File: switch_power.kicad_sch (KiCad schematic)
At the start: 0 parts

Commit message: CuPhy: adding ports
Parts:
- added U1: ~, Package_QFP:TQFP-128_14x14mm_P0.4mm, symbol lan9645xF:lan9645xF_128_TQFP

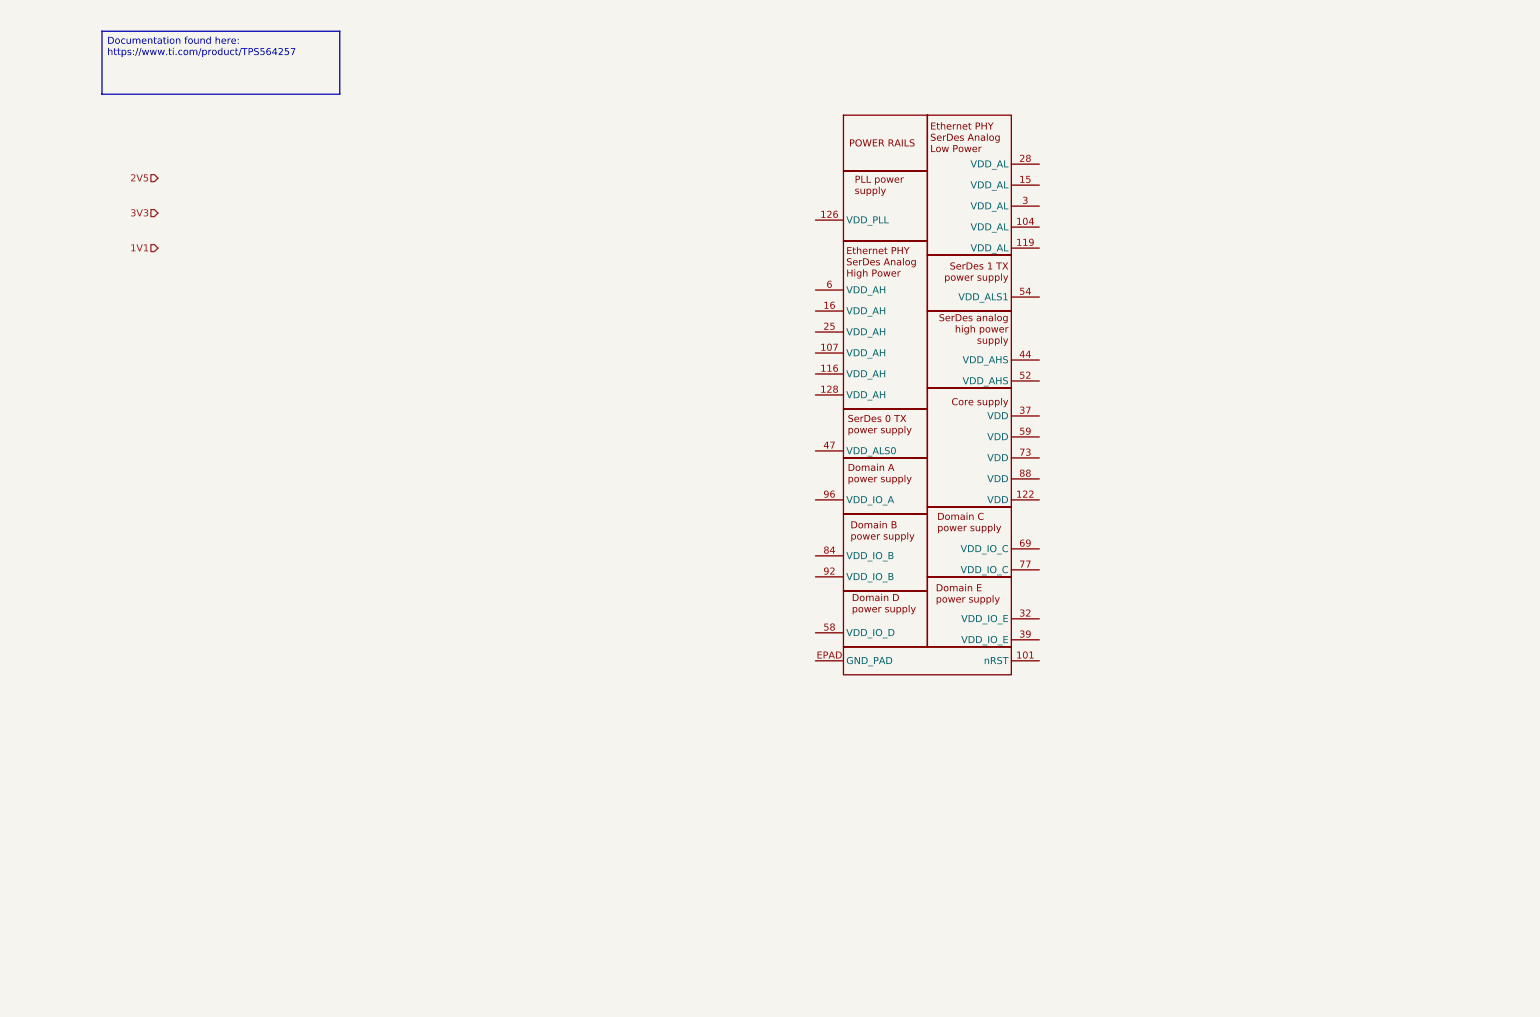
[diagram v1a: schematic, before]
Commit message: schematics: fixing the voltage rail and updating the files
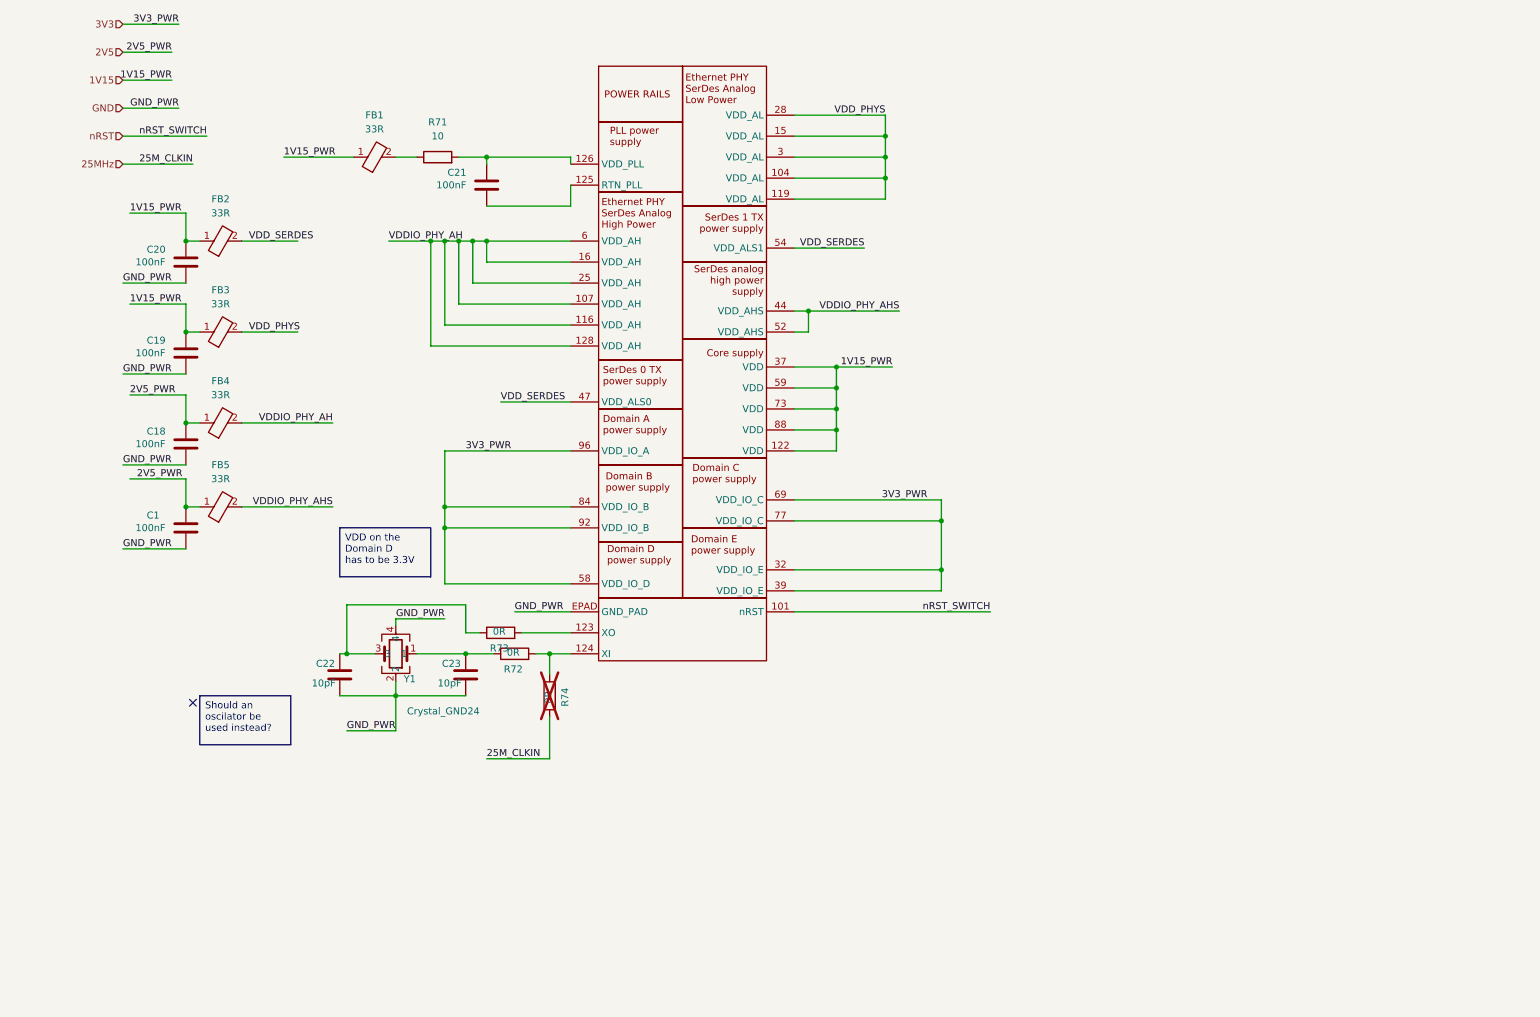
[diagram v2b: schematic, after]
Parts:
- added C1, C18, C19, C20, C21: 100nF, Capacitor_SMD:C_0201_0603Metric, symbol KL_C:C_100nF_35V_X7R_402_10
- added C22, C23: 10pF, Capacitor_SMD:C_0201_0603Metric, symbol KL_C:C_10pF_25V_C0G_0603_5
- added FB1, FB2, FB3, FB4, FB5: 33R, symbol KL_Ferrites:KL_FerritBead_33_3A
- added R71: 10, KL_Footprints:C_0603, symbol KL_R:R_10_100mW_0-1_0603
- added R72, R73, R74: 0R, KL_Footprints:C_0603, symbol KL_R:R_0R_250mW_0.5_0603
- added Y1: Crystal_GND24, symbol KL_Passive_ICs:Crystal_25MHz_32pF
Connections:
- net 2V5: now also C1.1, C18.1, FB4.1, FB5.1
- net 3V3: now also U1.32 (VDD_IO_E), U1.39 (VDD_IO_E), U1.58 (VDD_IO_D), U1.69 (VDD_IO_C), U1.77 (VDD_IO_C), U1.84 (VDD_IO_B), U1.92 (VDD_IO_B), U1.96 (VDD_IO_A)
- net nRST: now reaches U1.101 (nRST)
- net VDD_PHYS: now reaches U1.104 (VDD_AL)
- net VDD_PHYS: now also U1.119 (VDD_AL), U1.15 (VDD_AL), U1.28 (VDD_AL), U1.3 (VDD_AL), FB3.2
- net VDDIO_PHY_AH: now reaches U1.107 (VDD_AH)
- net VDDIO_PHY_AH: now also U1.116 (VDD_AH), U1.128 (VDD_AH), U1.16 (VDD_AH), U1.25 (VDD_AH), U1.6 (VDD_AH), FB4.2
- net 1V15: now reaches U1.122 (VDD)
- net 1V15: now also U1.37 (VDD), U1.59 (VDD), U1.73 (VDD), U1.88 (VDD), C19.1, C20.1, FB1.1, FB2.1, FB3.1
- net at U1.126 (VDD_PLL): now also C21.1, R71.2
- net VDDIO_PHY_AHS: now reaches U1.44 (VDD_AHS)
- net VDDIO_PHY_AHS: now also U1.52 (VDD_AHS), FB5.2
- net VDD_SERDES: now reaches U1.47 (VDD_ALS0)
- net VDD_SERDES: now also U1.54 (VDD_ALS1), FB2.2
- net GND: now reaches U1.EPAD (GND_PAD)
- net GND: now also C1.2, C18.2, C19.2, C20.2, C22.2, C23.2, Y1.2, Y1.4
- new net: FB1.2, R71.1
- new net: C21.2, U1.125 (RTN_PLL)
- new net: C23.1, R72.1, Y1.1
- new net: C22.1, R73.1, Y1.3
- new net: R73.2, U1.123 (XO)
- new net: R72.2, R74.2, U1.124 (XI)
- new net 25MHz: R74.1
- no-connect marks 0 -> 1

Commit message: switch: finished 1st version
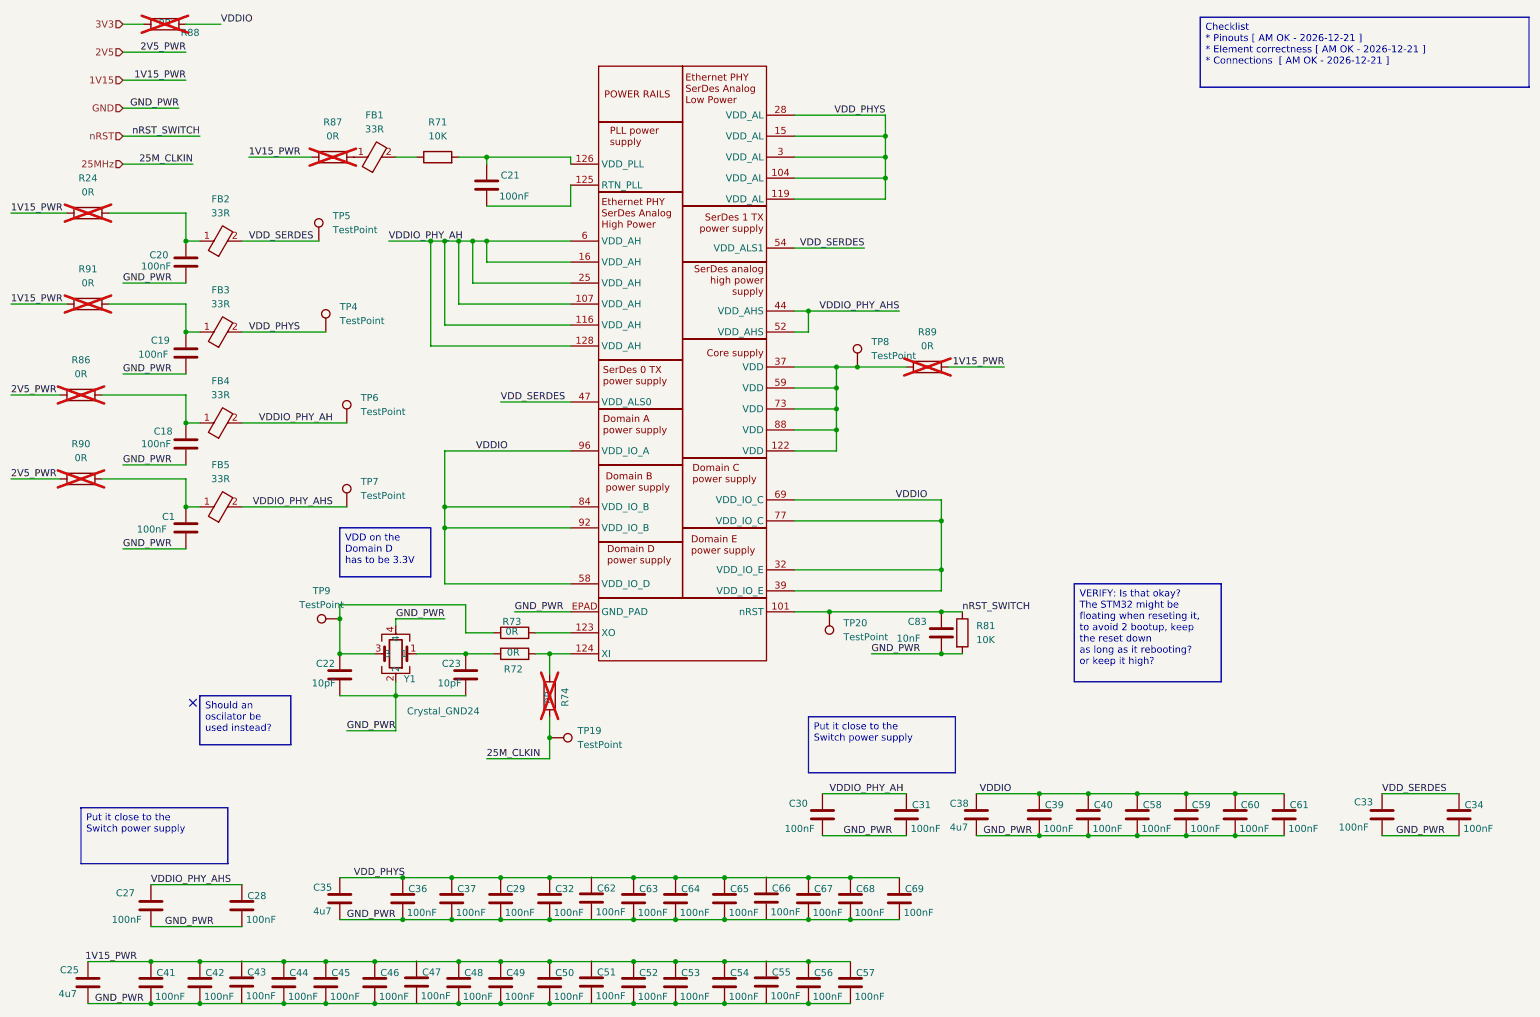
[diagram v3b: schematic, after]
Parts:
- removed C1, C18, C19, C20, C21: 100nF, Capacitor_SMD:C_0201_0603Metric, symbol KL_C:C_100nF_35V_X7R_402_10
- added C1, C18, C19, C20, C21: 100nF, KL:C_0402, symbol KL_C:C_100nF_35V_X7R_0402_10
- added C25, C35, C38: 4u7, KL:C_0603, symbol KL_C:C_4u7_10V_X5R_0603_10
- added C27, C28, C29, C30, C31, C32, C33, C34, C36, C37, C39, C40, C41, C42, C43, C44, C45, C46, C47, C48, C49, C50, C51, C52, C53, C54, C55, C56, C57, C58, C59, C60, C61, C62, C63, C64, C65, C66, C67, C68, C69: 100nF, KL:C_0603, symbol KL_C:C_100nF_16V_X7R_0603_10
- added C83: 10nF, KL:C_0603, symbol KL_C:C_10nF_25V_X7R_0603_20
- added R24, R86, R87, R88, R89, R90, R91: 0R, KL_Footprints:R_2512, symbol KL_R:R_0R_2W_5_2512
- added R81: 10K, KL:R_0603, symbol KL_R:R_10K_100mW_5_0603
- added TP19, TP20, TP4, TP5, TP6, TP7, TP8, TP9: TestPoint, symbol Connector:TestPoint
- C22, C23: footprint Capacitor_SMD:C_0201_0603Metric -> KL:C_0603
- FB1, FB2, FB3, FB4, FB5: footprint (none) -> KL:R_0603
- R71: value 10 -> 10K; footprint KL_Footprints:C_0603 -> KL:R_0603
- R72, R73, R74: footprint KL_Footprints:C_0603 -> KL:R_0603
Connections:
- net 1V15: now also C25.1, C41.1, C42.1, C44.1, C45.1, C46.1, C48.1, C49.1, C50.1, C52.1, C53.1, C54.1, C56.1, C57.1, R24.1, R87.1, R89.2, R91.1; no longer FB1.1, FB2.1, FB3.1, U1.122 (VDD), U1.37 (VDD), U1.59 (VDD), U1.73 (VDD), U1.88 (VDD)
- net 25MHz: now also TP19.1
- net 2V5: now also R86.1, R90.1; no longer FB4.1, FB5.1
- net 3V3: now also R88.1; no longer U1.32 (VDD_IO_E), U1.39 (VDD_IO_E), U1.58 (VDD_IO_D), U1.69 (VDD_IO_C), U1.77 (VDD_IO_C), U1.84 (VDD_IO_B), U1.92 (VDD_IO_B), U1.96 (VDD_IO_A)
- net GND: now also C1.2, C18.2, C19.2, C20.2, C25.2, C27.2, C28.2, C29.2, C30.2, C31.2, C32.2, C33.2, C34.2, C35.2, C36.2, C37.2, C38.2, C39.2, C40.2, C41.2, C42.2, C44.2, C45.2, C46.2, C48.2, C49.2, C50.2, C52.2, C53.2, C54.2, C56.2, C57.2, C58.2, C59.2, C60.2, C61.2, C63.2, C64.2, C65.2, C67.2, C68.2, C69.2, C83.2, R81.2
- net VDDIO_PHY_AH: now also C30.1, C31.1, TP6.1
- net VDDIO_PHY_AHS: now also C27.1, C28.1, TP7.1
- net VDD_PHYS: now also C29.1, C32.1, C35.1, C36.1, C37.1, C63.1, C64.1, C65.1, C67.1, C68.1, C69.1, TP4.1
- net VDD_SERDES: now also C33.1, C34.1, TP5.1
- net nRST: now also C83.1, R81.1, TP20.1
- net at R71.2, U1.126 (VDD_PLL): now also C21.1
- net at U1.125 (RTN_PLL): now also C21.2
- net at C22.1, R73.1, Y1.3: now also TP9.1
- new net: C1.1, FB5.1, R90.2
- new net: C19.1, FB3.1, R91.2
- new net: R89.1, TP8.1, U1.122 (VDD), U1.37 (VDD), U1.59 (VDD), U1.73 (VDD), U1.88 (VDD)
- new net: C20.1, FB2.1, R24.2
- new net: C18.1, FB4.1, R86.2
- new net: FB1.1, R87.2
- new net VDDIO: C38.1, C39.1, C40.1, C58.1, C59.1, C60.1, C61.1, R88.2, U1.32 (VDD_IO_E), U1.39 (VDD_IO_E), U1.58 (VDD_IO_D), U1.69 (VDD_IO_C), U1.77 (VDD_IO_C), U1.84 (VDD_IO_B), U1.92 (VDD_IO_B), U1.96 (VDD_IO_A)
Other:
- company: Kebag-Logic <contact@kebag-logic.com. -> Kebag-Logic <contact@kebag-logic.com>
- title: Power Switch -> Switch Power Sourcing
- moved on the sheet: R73

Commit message: minor footprint fixing
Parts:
- U1: footprint Package_QFP:TQFP-128_14x14mm_P0.4mm -> KL:TQFP-128_14x14mm_P0.4mm_with_EPAD; symbol lan9645xF:lan9645xF_128_TQFP -> KL_IC_LAN9645xF:lan9645xF_128_TQFP; Digikey (none) -> 150-LAN96455FT-I/8MWTR-ND; Mouser (none) -> 579-LAN96455FTI8MW; manf# LAN96455F-I/8MW -> (none)
- Y1: manf# VXM7-9032-25M0000000 -> (none)
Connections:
- net at R73.2: now also U1.124 (XO); no longer U1.123 (XO)
- net at R72.2, R74.2: now also U1.123 (XI); no longer U1.124 (XI)
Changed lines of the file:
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@@
 		(comment 1 "Confidential")
 	)
+	(text_box "WARNING: \nMake sure that the LEDS in the PHY part are connected to the right pwoer"
+		(exclude_from_sim no)
+		(at 170.18 85.09 0)
+		(size 35.56 11.43)
+		(margins 0.9525 0.9525 0.9525 0.9525)
+		(stroke
+			(width 0)
+			(type solid)
+		)
+		(fill
+			(type none)
+		)
+		(effects
+			(font
+				(size 1.27 1.27)
+			)
+			(justify left top)
+		)
+	)
 	(text_box "Put it close to the Switch power supply"
 		(exclude_from_sim no)
@@
 	)
 	(symbol
-		(lib_id "lan9645xF:lan9645xF_128_TQFP")
+		(lib_id "KL_IC_LAN9645xF:lan9645xF_128_TQFP")
 		(at 114.3 43.18 0)
 		(unit 1)
@@
 			)
 		)
-		(property "Footprint" "Package_QFP:TQFP-128_14x14mm_P0.4mm"
-			(at 114.3 43.18 0)
+		(property "Footprint" "KL:TQFP-128_14x14mm_P0.4mm_with_EPAD"
+			(at 128.016 37.338 0)
 			(effects
 				(font
@@
 			)
 		)
-		(property "manf#" "LAN96455F-I/8MW"
+		(property "Mouser" "579-LAN96455FTI8MW "
+			(at 127.254 35.052 0)
+			(effects
+				(font
+					(size 1.27 1.27)
+				)
+				(hide yes)
+			)
+		)
+		(property "Digikey" "150-LAN96455FT-I/8MWTR-ND"
+			(at 114.3 43.18 0)
+			(effects
+				(font
+					(size 1.27 1.27)
+				)
+				(hide yes)
+			)
+		)
+		(property "LSCS" ""
 			(at 114.3 43.18 0)
 			(effects
@@
 			)
 		)
-		(property "Datasheet" "~"
-			(at 78.74 138.43 0)
-			(effects
-				(font
-					(size 1.27 1.27)
-				)
-				(hide yes)
-			)
-		)
-		(property "Description" "Four pin crystal, GND on pins 2 and 4"
+		(property "Datasheet" ""
 			(at 78.74 138.43 0)
 			(effects
@@
 			)
 		)
-		(property "manf#" " VXM7-9032-25M0000000 "
+		(property "Description" ""
 			(at 78.74 138.43 0)
 			(effects

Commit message: This commit intends to fix multiple issues:
 - 1.1 -> 1.15 v buck rails
 - Revision consistently using Rev. A
 - Issue with the Switch symbol when moving library
 - Adding new footprint and symbol for 2.54mm Headers
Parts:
- U1: footprint KL:TQFP-128_14x14mm_P0.4mm_with_EPAD -> Package_QFP:TQFP-128_14x14mm_P0.4mm; Digikey 150-LAN96455FT-I/8MWTR-ND -> (none); Mouser 579-LAN96455FTI8MW -> (none); manf# (none) -> LAN96455F-I/8MW
